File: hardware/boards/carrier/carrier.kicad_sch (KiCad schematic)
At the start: 2 parts, among them J1 XT30PW(2+2)-M.G.B_SLOT

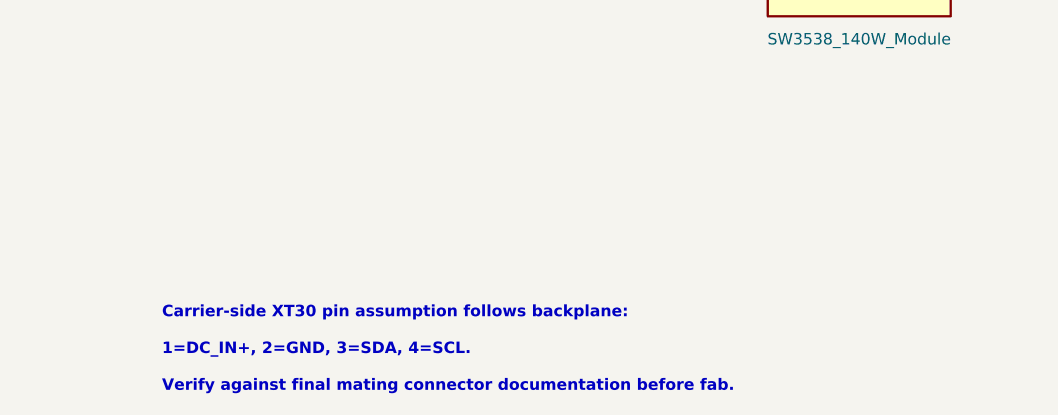
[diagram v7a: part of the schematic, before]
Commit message: Document carrier power switching architecture
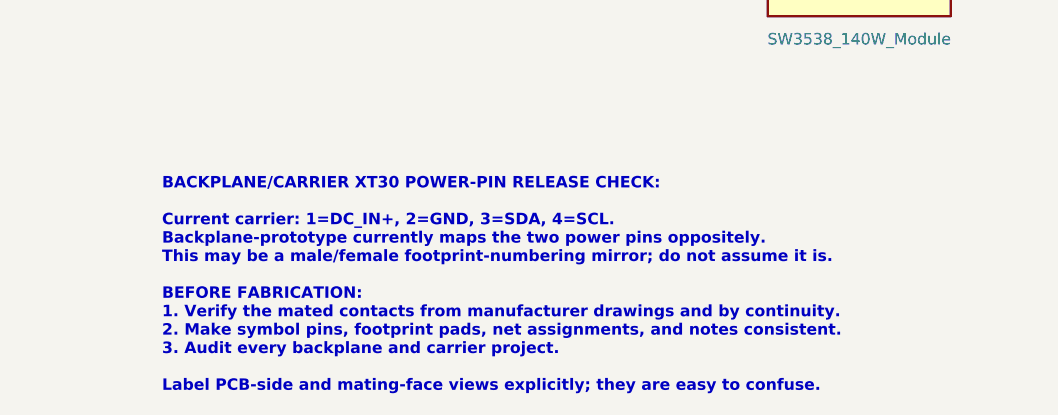
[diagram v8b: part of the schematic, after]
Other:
- note added: "BACKPLANE/CARRIER XT30 POWER-PIN RELEASE CHECK: Current carrier: 1=DC_IN+, 2=GND, 3=SDA, 4=SCL. Backplane-prototype currently maps the two power pins oppositely. This may be a male/female footprint-numbering mirror; do not assume it is. BEFORE FABRICATION: 1. Verify the mated contacts from manufacturer drawings and by continuity. 2. Make symbol pins, footprint pads, net assignments, and notes con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"
- note removed: "Carrier-side XT30 pin assumption follows backplane: 1=DC_IN+, 2=GND, 3=SDA, 4=SCL. Verify against final mating connector documentation before fab."
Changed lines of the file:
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@@
 		(rev "A")
 	)
-	(text "Carrier-side XT30 pin assumption follows backplane: \n\n1=DC_IN+, 2=GND, 3=SDA, 4=SCL. \n\nVerify against final mating connector documentation before fab."
+	(text "BACKPLANE/CARRIER XT30 POWER-PIN RELEASE CHECK:\n\nCurrent carrier: 1=DC_IN+, 2=GND, 3=SDA, 4=SCL.\nBackplane-prototype currently maps the two power pins oppositely.\nThis may be a male/female footprint-numbering mirror; do not assume it is.\n\nBEFORE FABRICATION:\n1. Verify the mated contacts from manufacturer drawings and by continuity.\n2. Make symbol pins, footprint pads, net assignments, and notes consistent.\n3. Audit every backplane and carrier project.\n\nLabel PCB-side and mating-face views explicitly; they are easy to confuse."
 		(exclude_from_sim no)
 		(at 35.56 82.55 0)
